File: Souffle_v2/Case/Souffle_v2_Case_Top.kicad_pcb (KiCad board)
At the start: 2 copper layers, 137.1 x 109.2 mm, 5 parts

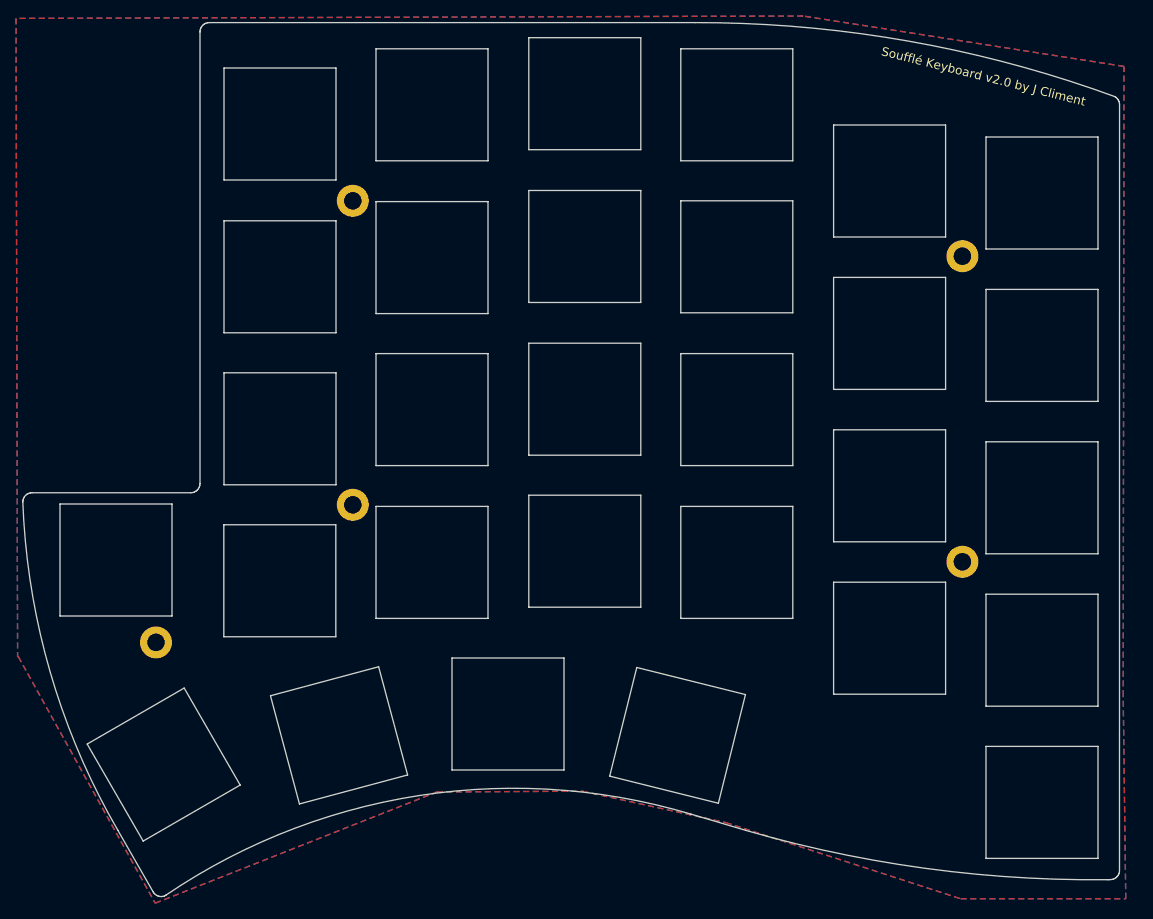
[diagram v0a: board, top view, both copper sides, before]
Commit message: Small fix for 2u keys in the thumb cluster touching the OLED key.
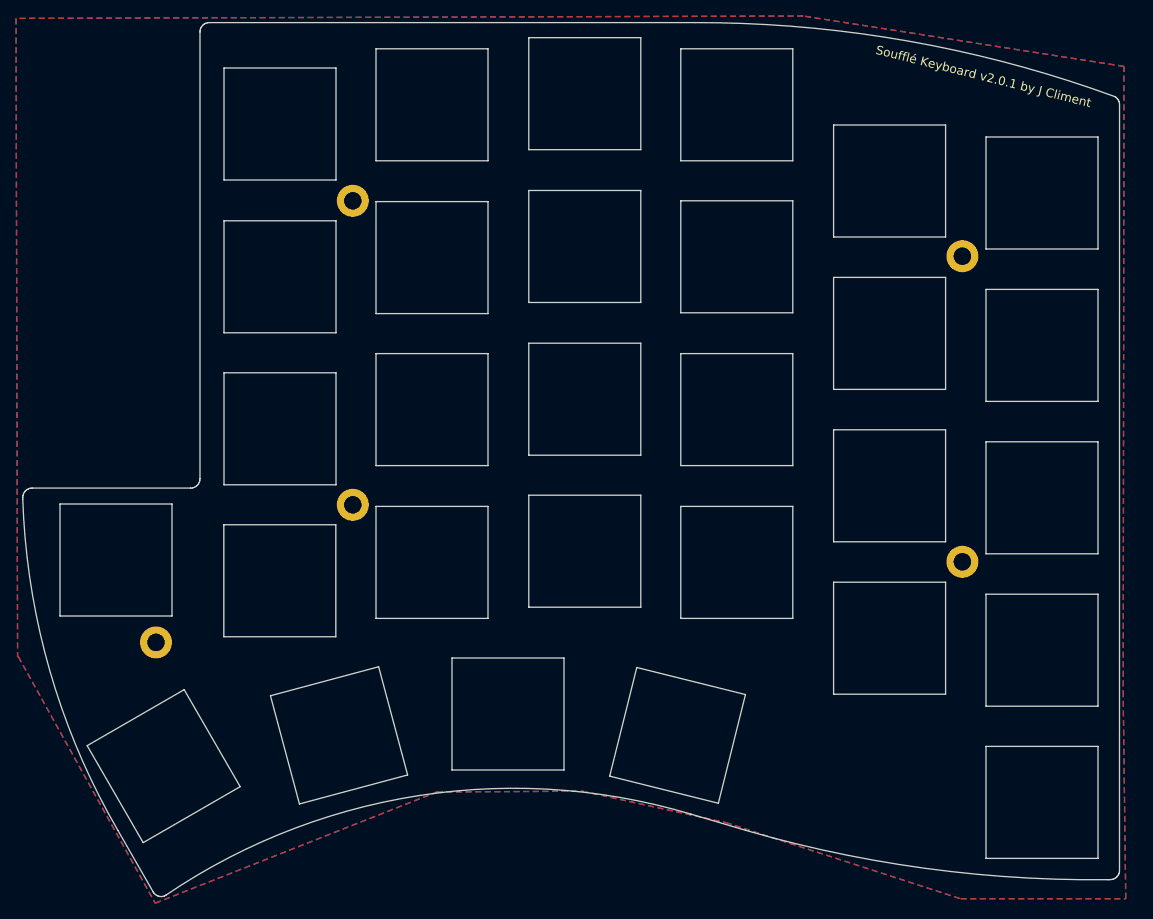
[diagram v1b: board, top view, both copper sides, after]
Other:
- outline, holes or cut-outs redrawn
- board text added: "Soufflé Keyboard v2.0.1 by J Climent"
- board text removed: "Soufflé Keyboard v2.0 by J Climent"
